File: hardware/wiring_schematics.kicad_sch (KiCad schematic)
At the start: 16 parts

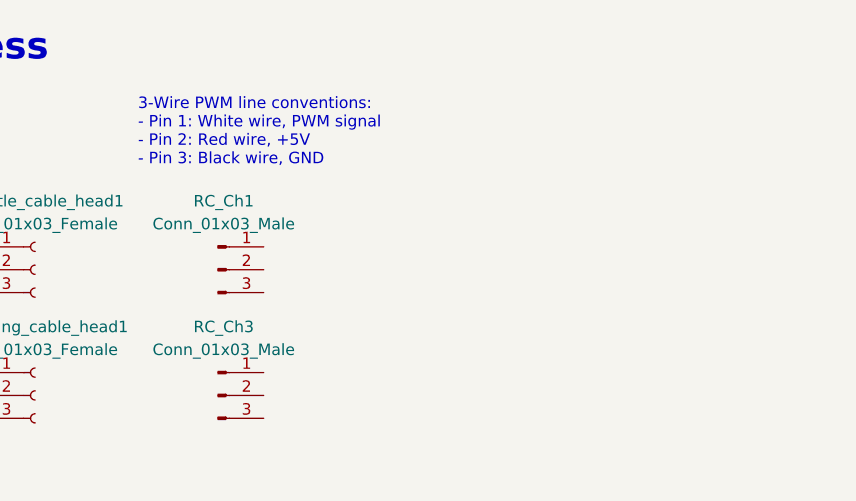
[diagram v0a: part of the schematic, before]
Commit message: added battery management docs, updated deadman switch assignment
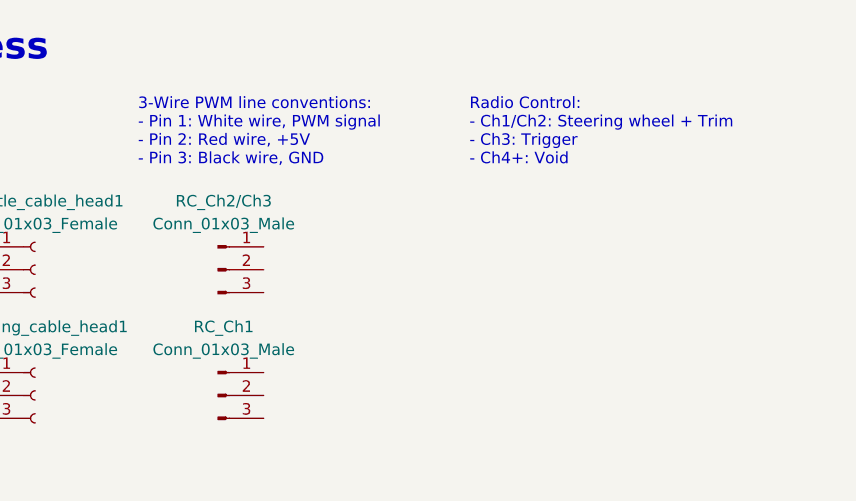
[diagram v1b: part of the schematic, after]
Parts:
- renumbered RC_Ch3 to RC_Ch1, RC_Ch1 to RC_Ch2/Ch3
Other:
- note added: "Radio Control: - Ch1/Ch2: Steering wheel + Trim - Ch3: Trigger - Ch4+: Void"
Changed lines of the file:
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@@
+    (effects (font (size 1.27 1.27)) (justify left bottom))
+  )
+  (text "Radio Control:\n- Ch1/Ch2: Steering wheel + Trim\n- Ch3: Trigger\n- Ch4+: Void"
+    (at 194.31 35.56 0)
     (effects (font (size 1.27 1.27)) (justify left bottom))
   )
@@
   (symbol (lib_id "Connector:Conn_01x03_Male") (at 166.37 60.96 0) (unit 1)
     (in_bom yes) (on_board yes) (fields_autoplaced)
-    (property "Reference" "RC_Ch3" (id 0) (at 167.005 53.34 0))
+    (property "Reference" "RC_Ch1" (id 0) (at 167.005 53.34 0))
     (property "Value" "Conn_01x03_Male" (id 1) (at 167.005 55.88 0))
     (property "Footprint" "" (id 2) (at 166.37 60.96 0)
@@
   (symbol (lib_id "Connector:Conn_01x03_Male") (at 166.37 46.99 0) (unit 1)
     (in_bom yes) (on_board yes) (fields_autoplaced)
-    (property "Reference" "RC_Ch1" (id 0) (at 167.005 39.37 0))
+    (property "Reference" "RC_Ch2/Ch3" (id 0) (at 167.005 39.37 0))
     (property "Value" "Conn_01x03_Male" (id 1) (at 167.005 41.91 0))
     (property "Footprint" "" (id 2) (at 166.37 46.99 0)
@@
       (reference "MPU_6050_Module") (unit 1) (value "Conn_01x08_Male_Stub") (footprint "")
     )
+    (path "/00e27c3e-a823-4f6f-b568-0697af3b0ee2"
+      (reference "RC_Ch1") (unit 1) (value "Conn_01x03_Male") (footprint "")
+    )
     (path "/dc2d99f5-d24a-4a43-93c5-d8a68bf9c6b0"
-      (reference "RC_Ch1") (unit 1) (value "Conn_01x03_Male") (footprint "")
-    )
-    (path "/00e27c3e-a823-4f6f-b568-0697af3b0ee2"
-      (reference "RC_Ch3") (unit 1) (value "Conn_01x03_Male") (footprint "")
+      (reference "RC_Ch2/Ch3") (unit 1) (value "Conn_01x03_Male") (footprint "")
     )
     (path "/57ed8993-e622-4edd-a033-210feb1c46a1"
